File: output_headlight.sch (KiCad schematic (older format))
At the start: 3 parts

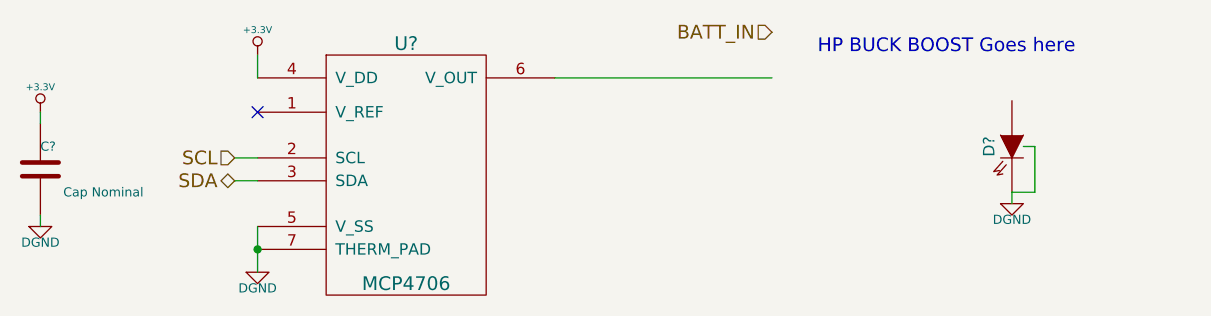
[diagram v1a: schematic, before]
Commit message: general organization, fixed power reg sheet, added jtag
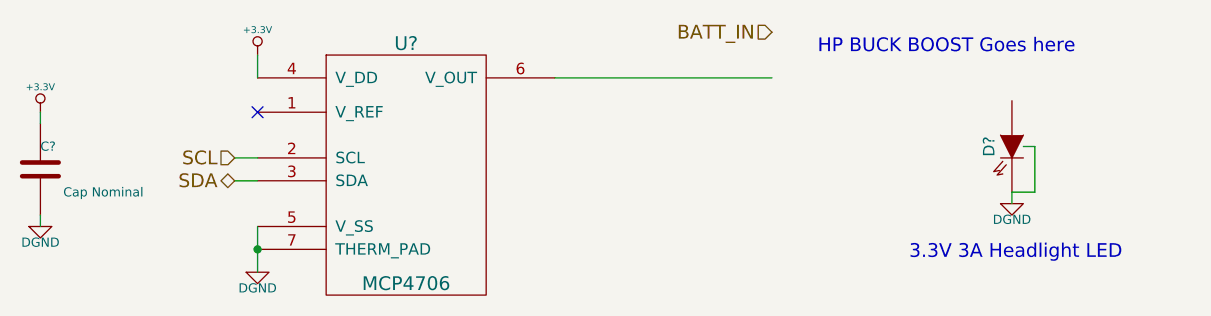
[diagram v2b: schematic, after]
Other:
- note added: "3.3V 3A Headlight LED"
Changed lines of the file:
@@
 $Descr A4 11693 8268
 encoding utf-8
-Sheet 17 17
+Sheet 16 18
 Title ""
 Date "8 dec 2013"
@@
 Text Notes 4600 1200 0    60   ~ 0
 HP BUCK BOOST Goes here
+Text Notes 5000 2100 0    60   ~ 0
+3.3V 3A Headlight LED
 $EndSCHEMATC
